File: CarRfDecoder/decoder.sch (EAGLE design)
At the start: 3 parts

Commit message: more changes in carRF
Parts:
- added C2, C3: 4.7uF, SparkFun-Capacitors:CAP0805
- added GND, USBD+, USBD-, USBV+, USBV+2, USBV-: (no value), wirepad:SMD2
- added R1, R2: 22, SparkFun-Resistors:RESISTOR0603-RES
- added R3, R4, R5: 2K, SparkFun-Resistors:RESISTOR0603-RES
- added U3: MCP73831, SparkFun-PowerIC:MCP73831
- added U6: MIC5219 3.3V, SparkFun-PowerIC:V_REG_MIC52193.3V
- renumbered U$1 to U1
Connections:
- new net A0: U1.PF7(ADC7)
- new net A1: U1.PF6(ADC6)
- new net A2: U1.PF5(ADC5)
- new net A3: U1.PF4(ADC4)
- new net A4: U1.PF1(ADC1)
- new net A5: R4.1, R5.2, U1.PF0(ADC0)
- new net D0: U1.PD2(RX)
- new net D1: U1.PD3(TX)
- new net D10: U1.PB6(ADC13)
- new net D11: U1.PB7
- new net D12: U1.PD6(ADC9)
- new net D13: U1.PC7
- new net D14: U1.PB0(SS)
- new net D15: U1.PB1(SCK)
- new net D16: U1.PB2(MOSI)
- new net D17: U1.PB3(MISO)
- new net D2: U1.PD1(SDA)
- new net D3: U1.PD0(SCL)
- new net D4: U1.PD4(ADC8)
- new net D5: U1.PC6
- new net D6: U1.PD7(ADC10)
- new net D7: U1.PE6, U3.STAT
- new net D8: U1.PB4(ADC11)
- new net D9: U1.PB5(ADC12)
- new net N$10: C2.1, R4.2, U3.VBAT, U6.EN, U6.IN, USBV+2.P
- new net N$11: R3.1, U3.PROG
- new net N$7: R2.1, USBD+.P
- new net N$8: R1.1, USBD-.P
- new net N$9: U3.VIN, USBV+.P
- new net TXLED: U1.PD5
- net D+: now also R2.2
- net D-: now also R1.2
- net GND: now also C2.2, C3.2, GND.P, R3.2, R5.1, U3.VSS, U6.GND, USBV-.P
- net VCC: now also C3.1, U6.OUT
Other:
- note added: "Battery level"

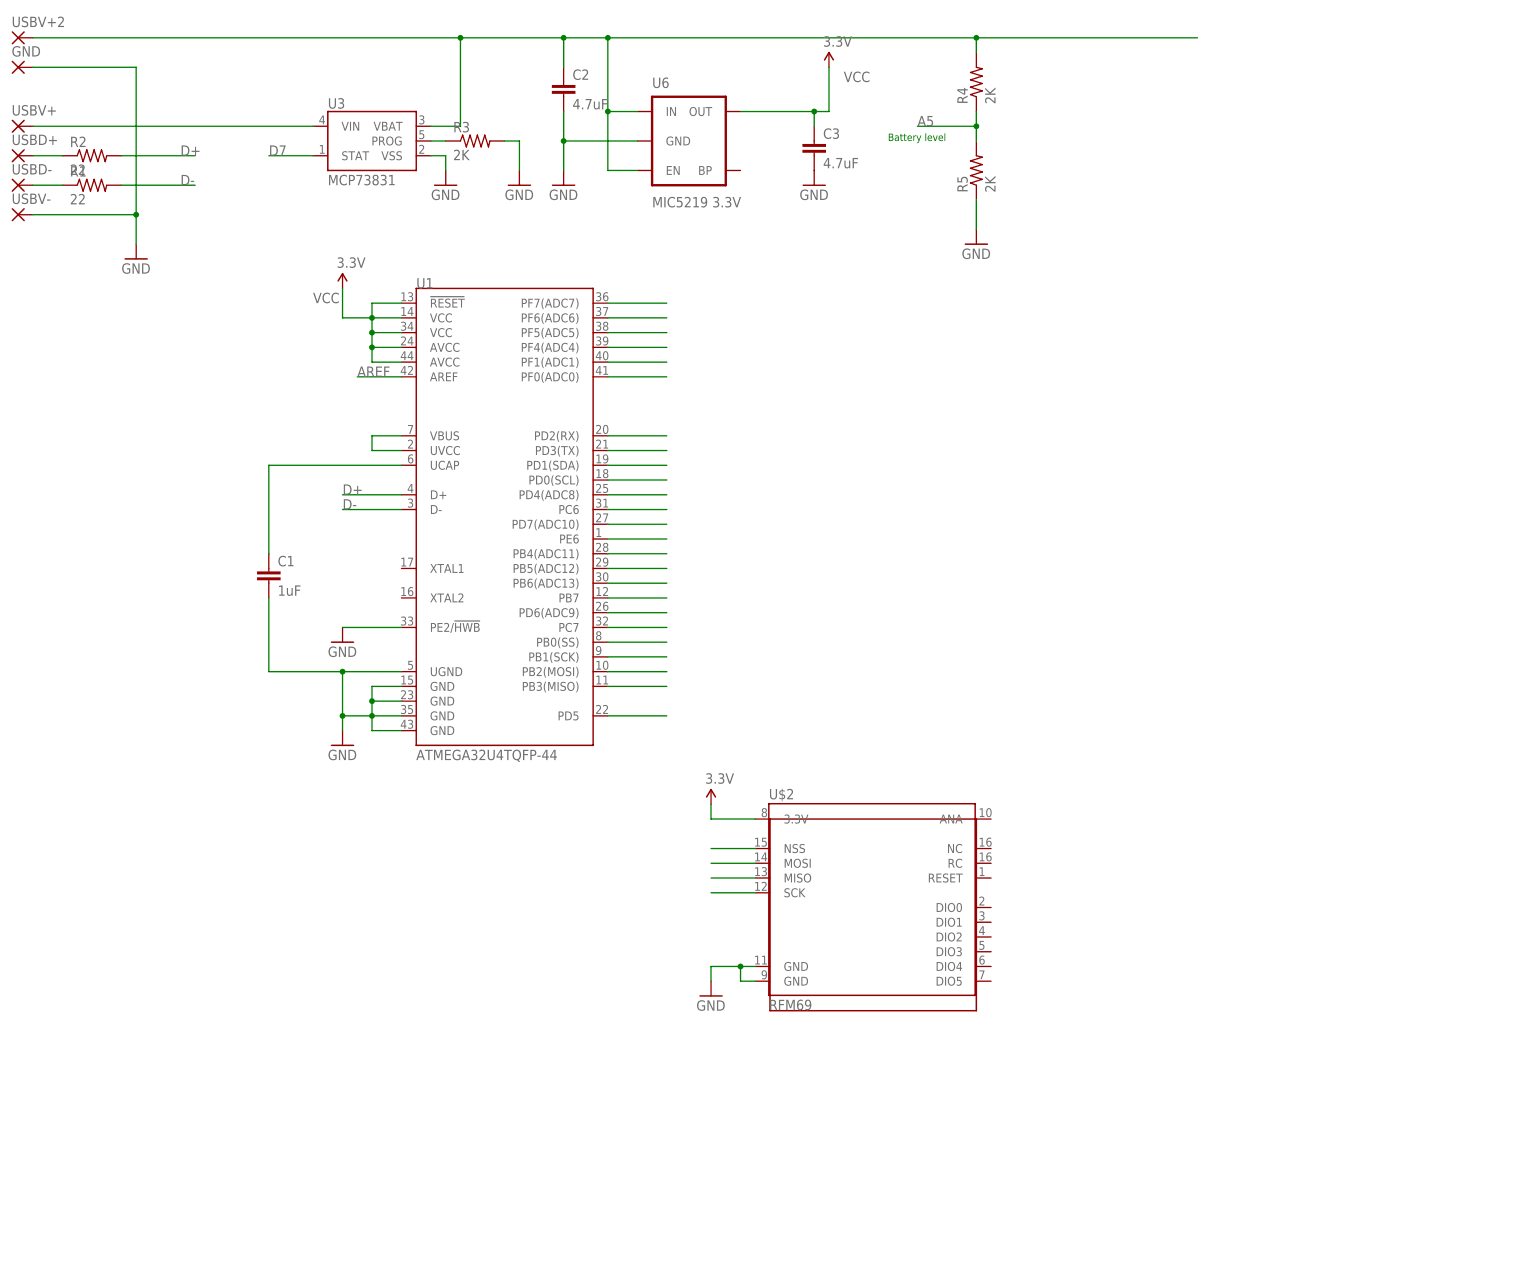
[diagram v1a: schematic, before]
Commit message: first version of car_decoder board
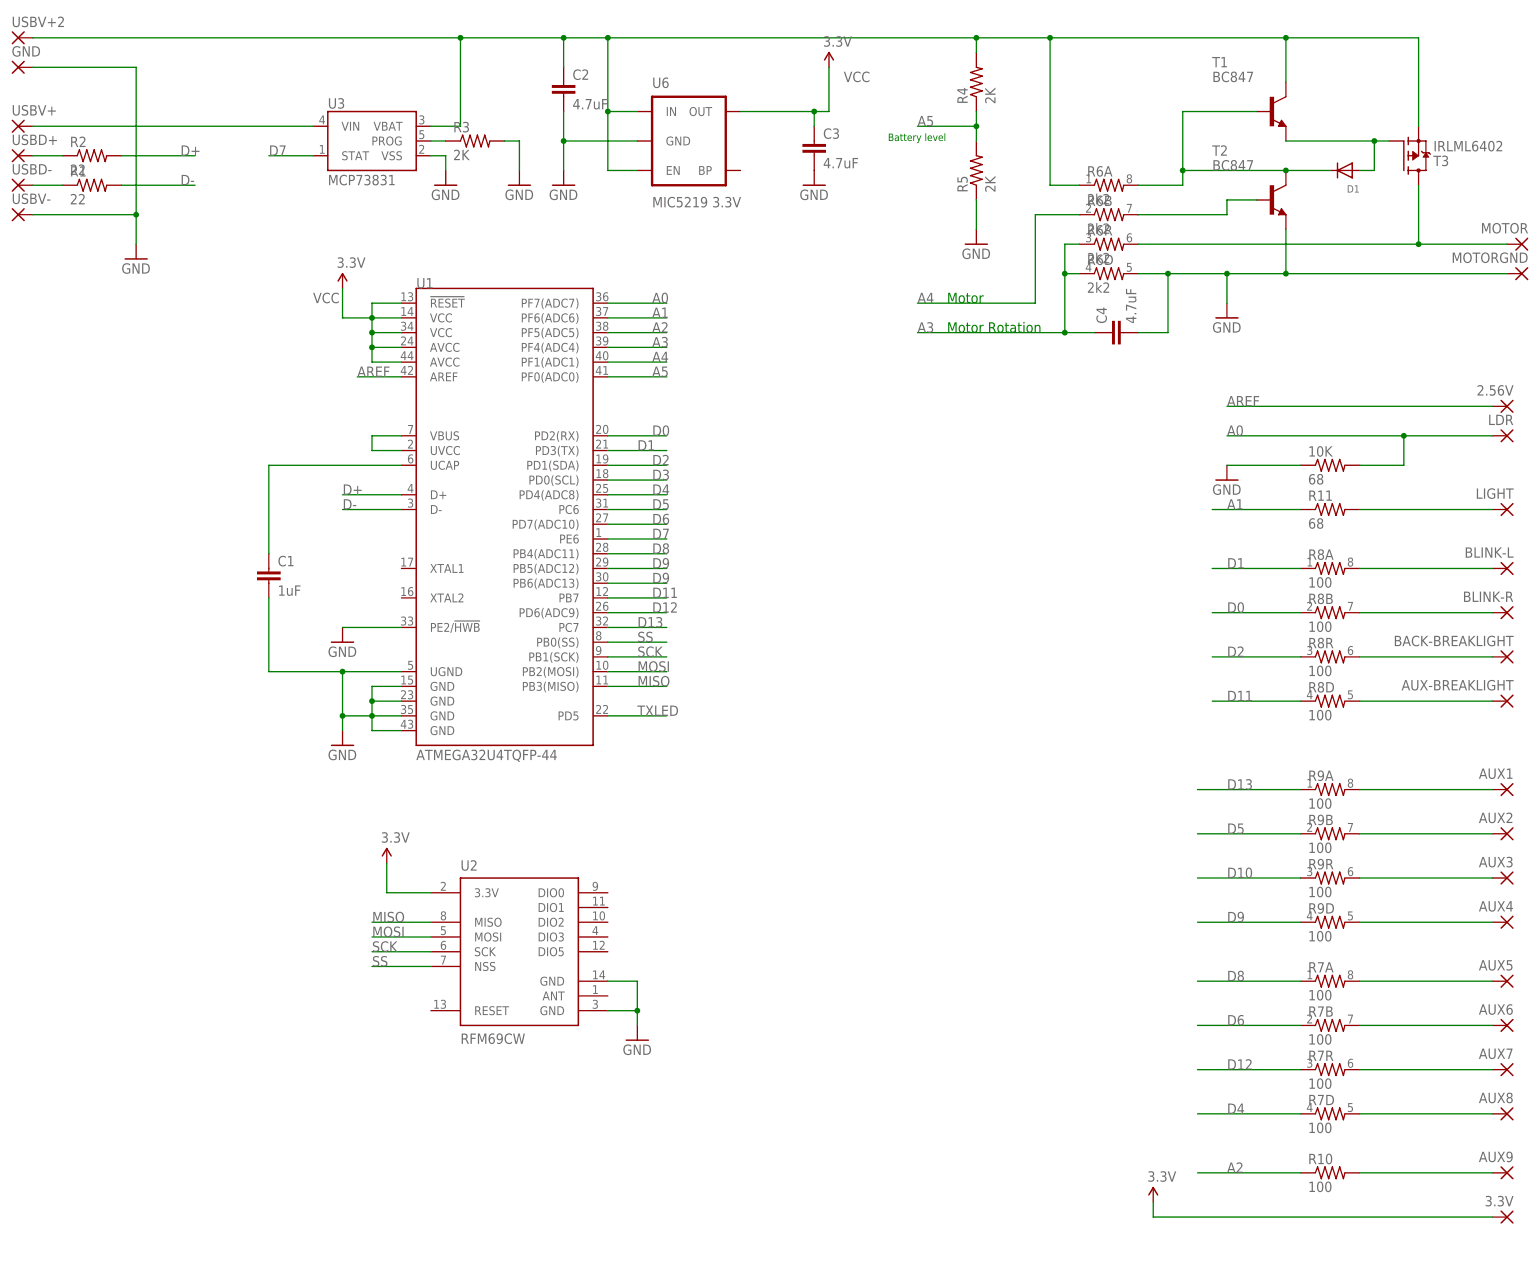
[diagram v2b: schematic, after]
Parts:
- removed U$2: RFM69, SWP:RFM69
- added 10K, R11: 68, SparkFun-Resistors:RESISTOR0603-RES
- added 2.56V, 3.3V, AUX-BREAKLIGHT, AUX1, AUX2, AUX3, AUX4, AUX5, AUX6, AUX7, AUX8, AUX9, BACK-BREAKLIGHT, BLINK-L, BLINK-R, LDR, LIGHT, MOTOR, MOTORGND: (no value), wirepad:SMD2
- added C4: 4.7uF, SparkFun-Capacitors:CAP0805
- added D1: (no value), adafruit:DIODESOD-523
- added R10: 100, SparkFun-Resistors:RESISTOR0603-RES
- added R6: 2k2, SparkFun-Resistors:RESISTOR-ARRAY0603-ARV
- added R7, R8, R9: 100, SparkFun-Resistors:RESISTOR-ARRAY0603-ARV
- added T1, T2: BC847, transistor:BC847
- added T3: IRLML6402, we-transistor:MOSFET-P-SOT23
- added U2: RFM69CW, SparkFun-RF:RFM69CW
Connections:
- removed net D14: U1.PB0(SS)
- removed net D15: U1.PB1(SCK)
- removed net D16: U1.PB2(MOSI)
- removed net D17: U1.PB3(MISO)
- removed net N$3: U$2.NSS
- removed net N$4: U$2.MOSI
- removed net N$5: U$2.MISO
- removed net N$6: U$2.SCK
- new net MISO: U1.PB3(MISO), U2.MISO
- new net MOSI: U1.PB2(MOSI), U2.MOSI
- new net N$12: LIGHT.P, R11.2
- new net N$13: BLINK-L.P, R8A.2
- new net N$14: D1.A, T1.E, T3.G
- new net N$15: MOTOR.P, R6R.2, T3.D
- new net N$16: BLINK-R.P, R8B.2
- new net N$17: R6B.2, T2.B
- new net N$18: BACK-BREAKLIGHT.P, R8R.2
- new net N$19: D1.C, R6A.2, T1.B, T2.C
- new net N$20: AUX-BREAKLIGHT.P, R8D.2
- new net N$21: AUX1.P, R9A.2
- new net N$22: AUX2.P, R9B.2
- new net N$23: AUX3.P, R9R.2
- new net N$24: AUX4.P, R9D.2
- new net N$25: AUX5.P, R7A.2
- new net N$26: AUX6.P, R7B.2
- new net N$27: AUX7.P, R7R.2
- new net N$28: AUX8.P, R7D.2
- new net N$29: AUX9.P, R10.2
- new net SCK: U1.PB1(SCK), U2.SCK
- new net SS: U1.PB0(SS), U2.NSS
- net A0: now also 10K.2, LDR.P
- net A1: now also R11.1
- net A2: now also R10.1
- net A3: now also C4.1, R6D.1, R6R.1
- net A4: now also R6B.1
- net AREF: now also 2.56V.P
- net D0: now also R8B.1
- net D1: now also R8A.1
- net D10: now also R9R.1
- net D11: now also R8D.1
- net D12: now also R7R.1
- net D13: now also R9A.1
- net D2: now also R8R.1
- net D4: now also R7D.1
- net D5: now also R9B.1
- net D6: now also R7B.1
- net D8: now also R7A.1
- net D9: now also R9D.1
- net GND: now also 10K.1, C4.2, MOTORGND.P, R6D.2, T2.E, U2.GND@1, U2.GND@2; no longer U$2.GND@1, U$2.GND@2
- net N$10: now also R6A.1, T1.C, T3.S
- net VCC: now also 3.3V.P, U2.3.3V; no longer U$2.3.3V
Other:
- note added: "Motor"
- note added: "Motor Rotation"

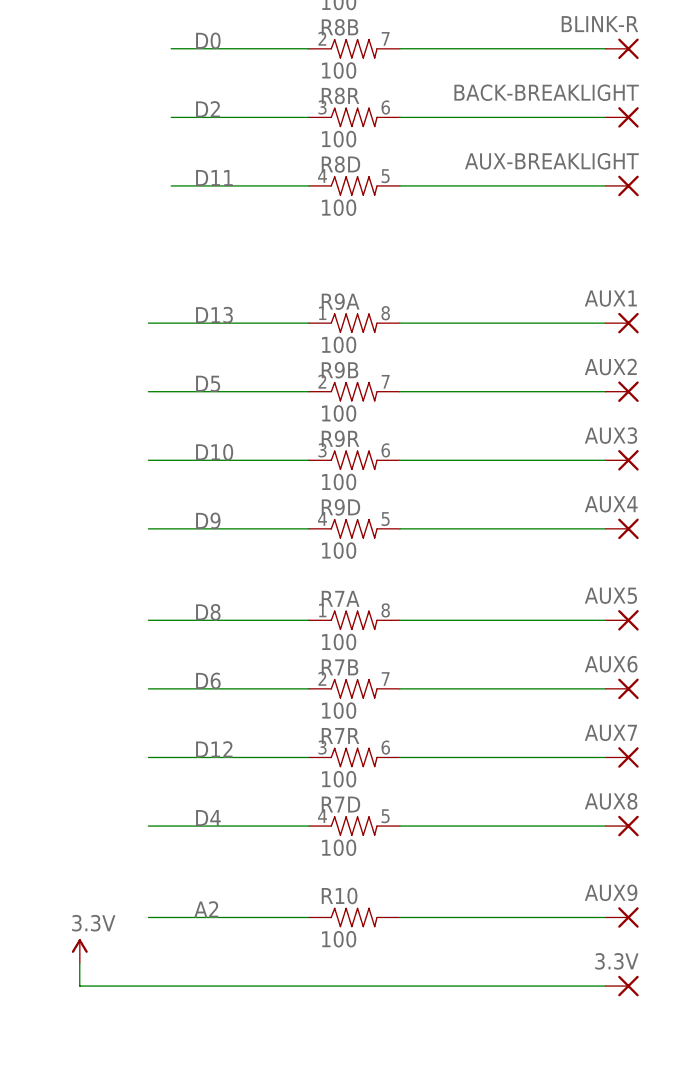
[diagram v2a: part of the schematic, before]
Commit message: added pin D3 to the board and changed the D11.
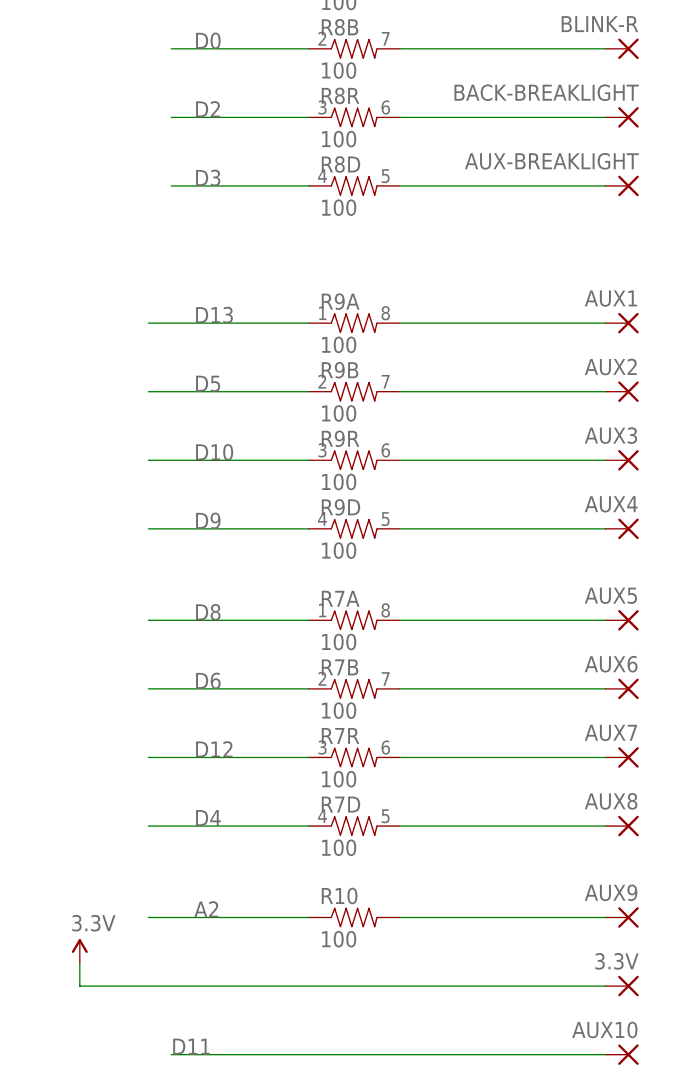
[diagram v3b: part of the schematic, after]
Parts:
- added AUX10: (no value), wirepad:SMD2
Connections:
- net D11: now also AUX10.P; no longer R8D.1
- net D3: now also R8D.1
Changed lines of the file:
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@@
 <part name="GND12" library="SparkFun-Aesthetics" deviceset="GND" device=""/>
 <part name="SUPPLY1" library="SparkFun-Aesthetics" deviceset="VCC" device="" value="3.3V"/>
+<part name="AUX10" library="wirepad" deviceset="SMD2" device=""/>
 </parts>
 <sheets>
@@
 <instance part="GND12" gate="1" x="71.12" y="-40.64"/>
 <instance part="SUPPLY1" gate="G$1" x="27.94" y="-10.16"/>
+<instance part="AUX10" gate="1" x="220.98" y="-78.74" rot="MR0"/>
 </instances>
 <busses>
@@
 <label x="73.66" y="55.88" size="1.778" layer="95"/>
 </segment>
+<segment>
+<pinref part="R8" gate="D" pin="1"/>
+<wire x1="185.42" y1="17.78" x2="170.18" y2="17.78" width="0.1524" layer="91"/>
+<label x="172.72" y="17.78" size="1.778" layer="95"/>
+</segment>
 </net>
 <net name="D4" class="0">
@@
 </segment>
 <segment>
-<pinref part="R8" gate="D" pin="1"/>
-<wire x1="185.42" y1="17.78" x2="170.18" y2="17.78" width="0.1524" layer="91"/>
-<label x="172.72" y="17.78" size="1.778" layer="95"/>
-</segment>
-</net>
+<pinref part="AUX10" gate="1" pin="P"/>
+<wire x1="218.44" y1="-78.74" x2="170.18" y2="-78.74" width="0.1524" layer="91"/>
+<label x="170.18" y="-78.74" size="1.778" layer="95"/>
+</segment>
+</net>

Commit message: car decoder
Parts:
- renumbered AUX-BREAKLIGHT to ABRKLIGHT, BACK-BREAKLIGHT to BBRKLIGHT
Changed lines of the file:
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@@
 <part name="BLINK-L" library="wirepad" deviceset="SMD2" device=""/>
 <part name="BLINK-R" library="wirepad" deviceset="SMD2" device=""/>
-<part name="BACK-BREAKLIGHT" library="wirepad" deviceset="SMD2" device=""/>
-<part name="AUX-BREAKLIGHT" library="wirepad" deviceset="SMD2" device=""/>
+<part name="BBRKLIGHT" library="wirepad" deviceset="SMD2" device=""/>
+<part name="ABRKLIGHT" library="wirepad" deviceset="SMD2" device=""/>
 <part name="AUX1" library="wirepad" deviceset="SMD2" device=""/>
 <part name="AUX2" library="wirepad" deviceset="SMD2" device=""/>
@@
 <instance part="BLINK-L" gate="1" x="220.98" y="40.64" rot="MR0"/>
 <instance part="BLINK-R" gate="1" x="220.98" y="33.02" rot="MR0"/>
-<instance part="BACK-BREAKLIGHT" gate="1" x="220.98" y="25.4" rot="MR0"/>
-<instance part="AUX-BREAKLIGHT" gate="1" x="220.98" y="17.78" rot="MR0"/>
+<instance part="BBRKLIGHT" gate="1" x="220.98" y="25.4" rot="MR0"/>
+<instance part="ABRKLIGHT" gate="1" x="220.98" y="17.78" rot="MR0"/>
 <instance part="AUX1" gate="1" x="220.98" y="2.54" rot="MR0"/>
 <instance part="AUX2" gate="1" x="220.98" y="-5.08" rot="MR0"/>
@@
 <segment>
 <pinref part="R8" gate="R" pin="2"/>
-<pinref part="BACK-BREAKLIGHT" gate="1" pin="P"/>
+<pinref part="BBRKLIGHT" gate="1" pin="P"/>
 <wire x1="195.58" y1="25.4" x2="218.44" y2="25.4" width="0.1524" layer="91"/>
 </segment>
@@
 <segment>
 <pinref part="R8" gate="D" pin="2"/>
-<pinref part="AUX-BREAKLIGHT" gate="1" pin="P"/>
+<pinref part="ABRKLIGHT" gate="1" pin="P"/>
 <wire x1="195.58" y1="17.78" x2="218.44" y2="17.78" width="0.1524" layer="91"/>
 </segment>
